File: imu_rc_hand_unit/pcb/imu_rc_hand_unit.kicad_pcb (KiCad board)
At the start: 2 copper layers, 35 x 50 mm, 80 parts, among them J1 USB_C_Receptacle_USB2.0_16P, J2 JST SH1.0, Q1 AO3400A, Q2 AO3400A, Q3 AO3401A, Q4 AO3400A, Q5 AO3401A, Q6 BSS138, Q7 2N2907A, Q8 2N2907A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

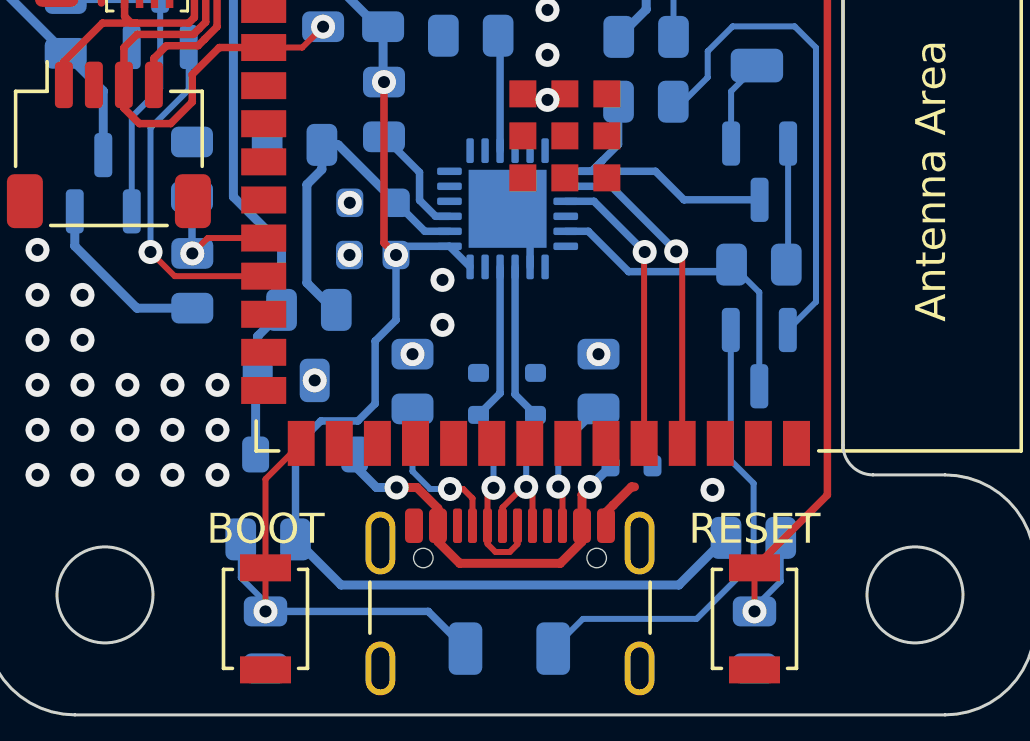
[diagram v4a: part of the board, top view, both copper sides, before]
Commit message: commit #13
refactored component values to more popular values
refactored components for less obsolete/more popular choices

bug fix TG1WDT_SYS_RESET
bug fix move() func

implement additional screen features
better readability
refactored navigation
added sensitivity option
added led information
added car status
added data print
added reset option

refactored board costs table
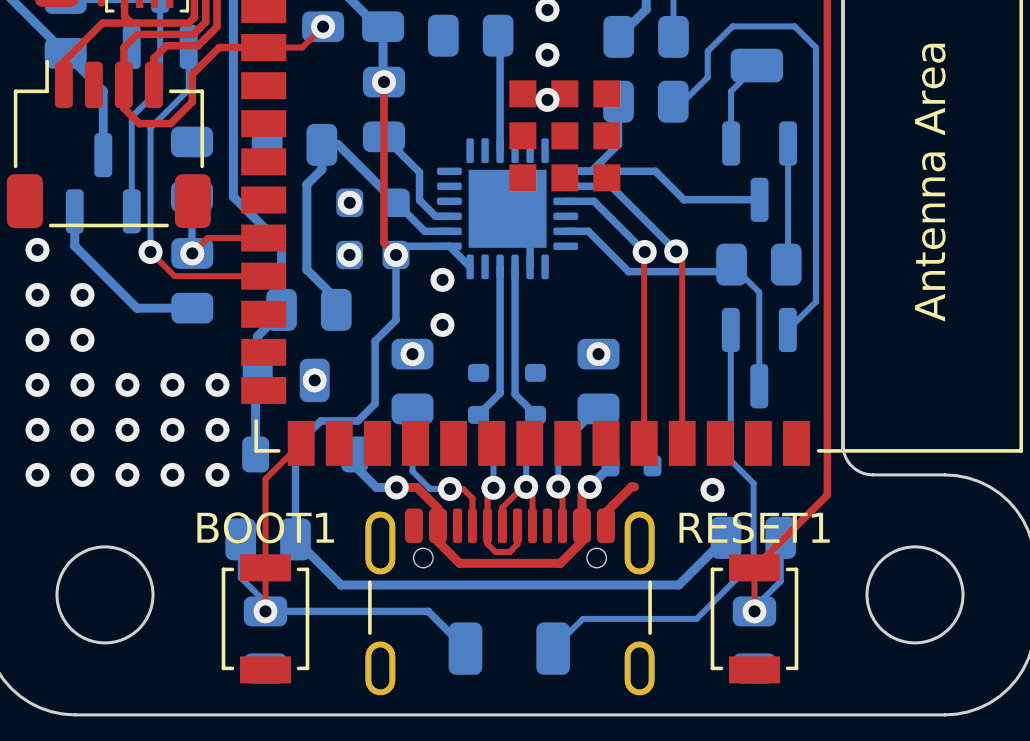
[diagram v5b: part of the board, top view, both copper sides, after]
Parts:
- C14, C15, C17, C18, C19, C20, C8: value 0.1uF/50V(10%) -> 100nF/50V(10%)
- D3: value LESD5D5.0CT1G -> ESD5B5V0WT
- Q1, Q2, Q4: value AO3400A -> IRLML6344TRPBF
- Q3, Q5: value AO3401A -> DMP3160L-7
- Q7, Q8: value 2N2907A -> BC817-25
- renumbered BOOT to BOOT1, RESET to RESET1
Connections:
- U6 pad 2: Net-(U6-GND-Pad2) -> GND
- U6 pad 25: Net-(U6-GND-Pad2) -> GND
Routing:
- net Net-(U6-GND-Pad2): track 2.25 -> 0.00 mm
- net GND: track 5.36 -> 7.61 mm
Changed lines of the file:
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@@
 	(net 82 "unconnected-(U6-~{RI}{slash}CLK-Pad1)")
 	(net 83 "unconnected-(U6-~{DSR}-Pad22)")
-	(net 84 "Net-(U6-GND-Pad2)")
-	(net 85 "unconnected-(U6-~{TXT}{slash}GPIO.0-Pad14)")
-	(net 86 "U0RXD")
-	(net 87 "unconnected-(U6-NC-Pad10)")
-	(net 88 "unconnected-(U6-~{WAKEUP}{slash}GPIO.3-Pad11)")
-	(net 89 "unconnected-(U6-VIO-Pad5)")
-	(net 90 "unconnected-(U6-~{RXT}{slash}GPIO.1-Pad13)")
-	(net 91 "unconnected-(U5-GPIO20{slash}U1CTS{slash}ADC2_CH9{slash}CLK_OUT1{slash}USB_D+-Pad14)")
-	(net 92 "unconnected-(U5-GPIO19{slash}U1RTS{slash}ADC2_CH8{slash}CLK_OUT2{slash}USB_D--Pad13)")
-	(net 93 "unconnected-(U5-GPIO48{slash}SPICLK_N{slash}SUBSPICLK_N_DIFF-Pad25)")
+	(net 84 "unconnected-(U6-~{TXT}{slash}GPIO.0-Pad14)")
+	(net 85 "U0RXD")
+	(net 86 "unconnected-(U6-NC-Pad10)")
+	(net 87 "unconnected-(U6-~{WAKEUP}{slash}GPIO.3-Pad11)")
+	(net 88 "unconnected-(U6-VIO-Pad5)")
+	(net 89 "unconnected-(U6-~{RXT}{slash}GPIO.1-Pad13)")
+	(net 90 "unconnected-(U5-GPIO20{slash}U1CTS{slash}ADC2_CH9{slash}CLK_OUT1{slash}USB_D+-Pad14)")
+	(net 91 "unconnected-(U5-GPIO19{slash}U1RTS{slash}ADC2_CH8{slash}CLK_OUT2{slash}USB_D--Pad13)")
+	(net 92 "unconnected-(U5-GPIO48{slash}SPICLK_N{slash}SUBSPICLK_N_DIFF-Pad25)")
 	(footprint "Button_Switch_SMD:SW_SPST_PTS647_Sx50"
 		(locked yes)
@@
 			)
 		)
-		(property "Value" "0.1uF/50V(10%)"
+		(property "Value" "100nF/50V(10%)"
 			(at 0 1.68 0)
 			(layer "F.Fab")
@@
 			)
 		)
-		(property "Value" "0.1uF/50V(10%)"
+		(property "Value" "100nF/50V(10%)"
 			(at 0 1.68 0)
 			(layer "F.Fab")
@@
 		(descr "Ultra-small-sized Tactile Switch with High Contact Reliability, Top-actuated Model, without Ground Terminal, without Boss")
 		(tags "Tactile Switch")
-		(property "Reference" "RESET"
+		(property "Reference" "RESET1"
 			(at 3 0 180)
 			(layer "F.SilkS")
@@
 			)
 		)
-		(property "Value" "0.1uF/50V(10%)"
+		(property "Value" "100nF/50V(10%)"
 			(at 0 1.68 0)
 			(layer "F.Fab")
@@
 		(descr "Ultra-small-sized Tactile Switch with High Contact Reliability, Top-actuated Model, without Ground Terminal, without Boss")
 		(tags "Tactile Switch")
-		(property "Reference" "BOOT"
+		(property "Reference" "BOOT1"
 			(at 3 0 180)
 			(layer "F.SilkS")
@@
 			)
 		)
-		(property "Value" "0.1uF/50V(10%)"
+		(property "Value" "100nF/50V(10%)"
 			(at 0 1.68 0)
 			(layer "F.Fab")
@@
 			)
 		)
-		(property "Value" "0.1uF/50V(10%)"
+		(property "Value" "100nF/50V(10%)"
 			(at 0 1.68 90)
 			(layer "F.Fab")
@@
 			(size 1.5 0.9)
 			(layers "F.Cu" "F.Paste" "F.Mask")
-			(net 92 "unconnected-(U5-GPIO19{slash}U1RTS{slash}ADC2_CH8{slash}CLK_OUT2{slash}USB_D--Pad13)")
+			(net 91 "unconnected-(U5-GPIO19{slash}U1RTS{slash}ADC2_CH8{slash}CLK_OUT2{slash}USB_D--Pad13)")
 			(pinfunction "GPIO19/U1RTS/ADC2_CH8/CLK_OUT2/USB_D-")
 			(pintype "bidirectional+no_connect")
@@
 			(size 1.5 0.9)
 			(layers "F.Cu" "F.Paste" "F.Mask")
-			(net 91 "unconnected-(U5-GPIO20{slash}U1CTS{slash}ADC2_CH9{slash}CLK_OUT1{slash}USB_D+-Pad14)")
+			(net 90 "unconnected-(U5-GPIO20{slash}U1CTS{slash}ADC2_CH9{slash}CLK_OUT1{slash}USB_D+-Pad14)")
 			(pinfunction "GPIO20/U1CTS/ADC2_CH9/CLK_OUT1/USB_D+")
 			(pintype "bidirectional+no_connect")
@@
 			(size 1.5 0.9)
 			(layers "F.Cu" "F.Paste" "F.Mask")
-			(net 93 "unconnected-(U5-GPIO48{slash}SPICLK_N{slash}SUBSPICLK_N_DIFF-Pad25)")
+			(net 92 "unconnected-(U5-GPIO48{slash}SPICLK_N{slash}SUBSPICLK_N_DIFF-Pad25)")
 			(pinfunction "GPIO48/SPICLK_N/SUBSPICLK_N_DIFF")
 			(pintype "bidirectional+no_connect")
@@
 			(size 1.5 0.9)
 			(layers "F.Cu" "F.Paste" "F.Mask")
-			(net 86 "U0RXD")
+			(net 85 "U0RXD")
 			(pinfunction "U0RXD/GPIO44/CLK_OUT2")
 			(pintype "bidirectional")
@@
 			)
 		)
-		(property "Value" "AO3401A"
+		(property "Value" "DMP3160L-7"
 			(at 0 -2.4 90)
 			(layer "B.Fab")
@@
 			)
 		)
-		(property "Value" "AO3400A"
+		(property "Value" "IRLML6344TRPBF"
 			(at 0 -2.4 90)
 			(layer "B.Fab")
@@
 			)
 		)
-		(property "Value" "AO3400A"
+		(property "Value" "IRLML6344TRPBF"
 			(at 0 -2.4 90)
 			(layer "B.Fab")
@@
 			)
 		)
-		(property "Value" "0.1uF/50V(10%)"
+		(property "Value" "100nF/50V(10%)"
 			(at 0 -1.68 90)
 			(layer "B.Fab")
@@
 			)
 		)
-		(property "Value" "AO3400A"
+		(property "Value" "IRLML6344TRPBF"
 			(at 0 -2.4 0)
 			(layer "B.Fab")
@@
 			)
 		)
-		(property "Value" "LESD5D5.0CT1G"
+		(property "Value" "ESD5B5V0WT"
 			(at 0 -1.4 90)
 			(layer "B.Fab")
@@
 			)
 		)
-		(property "Value" "0.1uF/50V(10%)"
+		(property "Value" "100nF/50V(10%)"
 			(at 0 -1.68 90)
 			(layer "B.Fab")
@@
 			)
 		)
-		(property "Value" "2N2907A"
+		(property "Value" "BC817-25"
 			(at 0 -2.4 90)
 			(layer "B.Fab")
@@
 			)
 		)
-		(property "Value" "AO3401A"
+		(property "Value" "DMP3160L-7"
 			(at 0 -2.4 90)
 			(layer "B.Fab")
@@
 			)
 		)
-		(property "Value" "2N2907A"
+		(property "Value" "BC817-25"
 			(at 0 -2.4 90)
 			(layer "B.Fab")
@@
 			(layers "B.Cu" "B.Paste" "B.Mask")
 			(roundrect_rratio 0.25)
-			(net 84 "Net-(U6-GND-Pad2)")
+			(net 2 "GND")
 			(pinfunction "GND")
 			(pintype "power_in")
@@
 			(layers "B.Cu" "B.Paste" "B.Mask")
 			(roundrect_rratio 0.25)
-			(net 89 "unconnected-(U6-VIO-Pad5)")
+			(net 88 "unconnected-(U6-VIO-Pad5)")
 			(pinfunction "VIO")
 			(pintype "power_in+no_connect")
@@
 			(layers "B.Cu" "B.Paste" "B.Mask")
 			(roundrect_rratio 0.25)
-			(net 87 "unconnected-(U6-NC-Pad10)")
+			(net 86 "unconnected-(U6-NC-Pad10)")
 			(pinfunction "NC")
 			(pintype "no_connect")
@@
 			(layers "B.Cu" "B.Paste" "B.Mask")
 			(roundrect_rratio 0.25)
-			(net 88 "unconnected-(U6-~{WAKEUP}{slash}GPIO.3-Pad11)")
+			(net 87 "unconnected-(U6-~{WAKEUP}{slash}GPIO.3-Pad11)")
 			(pinfunction "~{WAKEUP}/GPIO.3")
 			(pintype "bidirectional+no_connect")
@@
 			(layers "B.Cu" "B.Paste" "B.Mask")
 			(roundrect_rratio 0.25)
-			(net 90 "unconnected-(U6-~{RXT}{slash}GPIO.1-Pad13)")
+			(net 89 "unconnected-(U6-~{RXT}{slash}GPIO.1-Pad13)")
 			(pinfunction "~{RXT}/GPIO.1")
 			(pintype "bidirectional+no_connect")
@@
 			(layers "B.Cu" "B.Paste" "B.Mask")
 			(roundrect_rratio 0.25)
-			(net 85 "unconnected-(U6-~{TXT}{slash}GPIO.0-Pad14)")
+			(net 84 "unconnected-(U6-~{TXT}{slash}GPIO.0-Pad14)")
 			(pinfunction "~{TXT}/GPIO.0")
 			(pintype "bidirectional+no_connect")
@@
 			(layers "B.Cu" "B.Paste" "B.Mask")
 			(roundrect_rratio 0.25)
-			(net 86 "U0RXD")
+			(net 85 "U0RXD")
 			(pinfunction "TXD")
 			(pintype "output")
@@
 			(property pad_prop_heatsink)
 			(layers "B.Cu" "B.Mask")
-			(net 84 "Net-(U6-GND-Pad2)")
+			(net 2 "GND")
 			(pinfunction "GND")
 			(pintype "passive")
@@
 	)
 	(segment
+		(start 38.42 53.88)
+		(end 37.67 53.13)
+		(width 0.25)
+		(layer "B.Cu")
+		(net 2)
+	)
+	(segment
+		(start 38.42 55.0675)
+		(end 38.42 53.88)
+		(width 0.25)
+		(layer "B.Cu")
+		(net 2)
+	)
+	(segment
 		(start 35.68 22.45)
 		(end 38.07 24.84)
@@
 	)
 	(segment
+		(start 31.96 56.14)
+		(end 31.96 56.58)
+		(width 0.3)
+		(layer "B.Cu")
+		(net 10)
+	)
+	(segment
 		(start 34.91 53.88)
 		(end 33.96 52.93)
@@
 	)
 	(segment
+		(start 30.98 52.32)
+		(end 30.98 55.16)
+		(width 0.3)
+		(layer "B.Cu")
+		(net 10)
+	)
+	(segment
 		(start 31.48 51.82)
 		(end 30.98 52.32)
@@
 	)
 	(segment
-		(start 33.96 52.93)
-		(end 32.03 51)
+		(start 30.98 55.16)
+		(end 31.96 56.14)
 		(width 0.3)
 		(layer "B.Cu")
@@
 	)
 	(segment
-		(start 30.98 55.6)
-		(end 31.96 56.58)
-		(width 0.3)
-		(layer "B.Cu")
-		(net 10)
-	)
-	(segment
-		(start 30.98 52.32)
-		(end 30.98 55.6)
+		(start 33.96 52.93)
+		(end 32.03 51)
 		(width 0.3)
 		(layer "B.Cu")
@@
 	)
 	(segment
-		(start 38.42 53.88)
-		(end 37.67 53.13)
-		(width 0.25)
-		(layer "B.Cu")
-		(net 84)
-	)
-	(segment
-		(start 38.42 55.0675)
-		(end 38.42 53.88)
-		(width 0.25)
-		(layer "B.Cu")
-		(net 84)
-	)
-	(segment
 		(start 42.22 54.59)
 		(end 42.22 60.95)
 		(width 0.2)
 		(layer "F.Cu")
-		(net 86)
+		(net 85)
 	)
 	(segment
@@
 		(width 0.2)
 		(layer "F.Cu")
-		(net 86)
+		(net 85)
 	)
 	(via
@@
 		(drill 0.4)
 		(layers "F.Cu" "B.Cu")
-		(net 86)
+		(net 85)
 	)
 	(segment
@@
 		(width 0.25)
 		(layer "B.Cu")
-		(net 86)
+		(net 85)
 	)
 	(segment
@@
 		(width 0.25)
 		(layer "B.Cu")
-		(net 86)
+		(net 85)
 	)
 	(zone

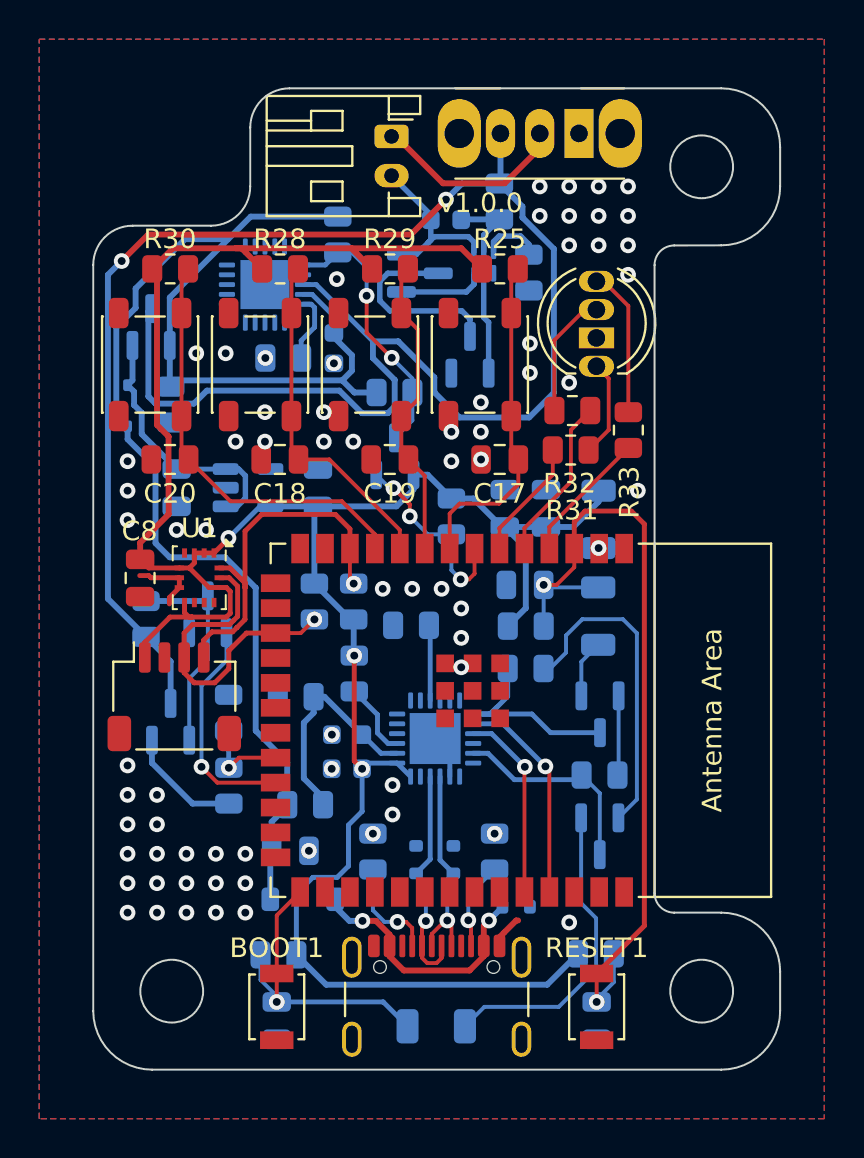
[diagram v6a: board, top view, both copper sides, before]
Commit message: commit #24
version 2 of proximity sensor case (better results)
updated all M2 holes in pcbs to 2.4mm diameter instead of 2.2mm
updated all M3 holes in pcbs to 3.4mm diameter instead of 3.2mm
minor changes to encoder board
gerber files encoder board
first revision in hand unit
added prox sensor test unit (for test purposes)
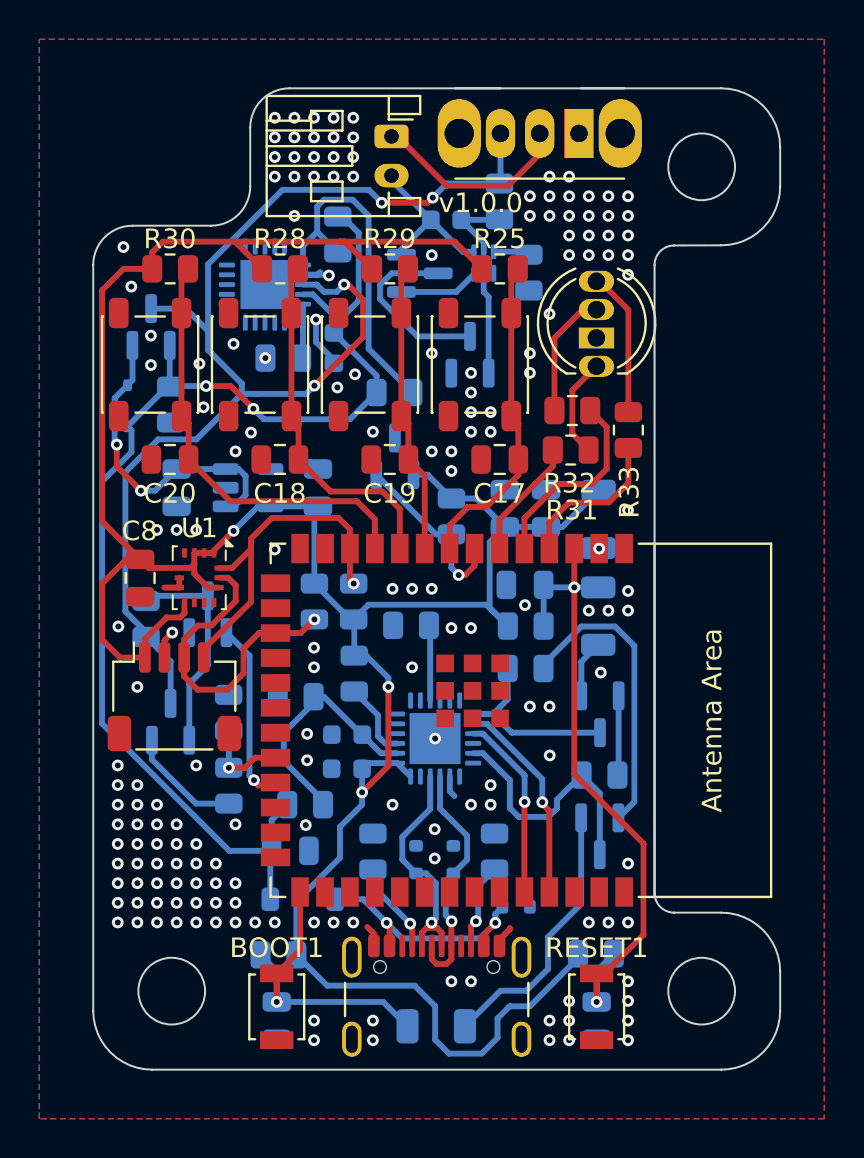
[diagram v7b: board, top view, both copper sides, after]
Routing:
- net +BATT: track 97.9 -> 63.6 mm, vias 2 -> 4
- net +3.3V: track 126.1 -> 142.0 mm
- net VBUS: track 74.5 -> 63.1 mm, vias 0 -> 2
- net CHIP_PU: track 41.4 -> 33.5 mm
- net CHRG_5V: track 13.8 -> 20.5 mm, vias 2 -> 0
- net RTS: track 13.8 -> 9.49 mm
- net GND: track 7.61 -> 10.9 mm, vias 71 -> 176
- net Net-(D6-K): track 13.4 -> 16.5 mm, vias 0 -> 2
- net DTR: track 10.6 -> 13.3 mm
- net Net-(Q8-C): track 15.9 -> 13.8 mm
- net BATT_READ_EN: track 11.5 -> 9.40 mm
- net LED_GREEN: track 8.42 -> 10.1 mm
- net Net-(D3-A2): track 10.8 -> 12.3 mm
- net Net-(U3-V-): track 3.13 -> 1.86 mm
- net Net-(Q8-B): track 16.4 -> 15.1 mm
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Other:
- outline, holes or cut-outs redrawn
- board text added: "{ "ViaStitching": "0.2", "stitch_zone_0": { "HSpacing": "1", "VSpacing": "1", "HOffset": "0", "VOffset": "0", "Clearance": "0.2", "Randomize": false } }"

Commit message: commit #25
added library for mouse-bites
minor changes in prox sensors board
added necessary changes for test unit to print
minor changes in hand unit
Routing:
- net GND: track 10.9 -> 16.9 mm, vias 176 -> 166
- net +3.3V: track 142.0 -> 143.3 mm
